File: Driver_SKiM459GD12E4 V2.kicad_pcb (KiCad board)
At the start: 4 copper layers, 169.2 x 116 mm, 339 parts, among them J1 2-338069-0, J13 EL1, J14 GL1, J15 NTC1_A, J16 NTC1_B, J17 GH1, J18 OUT1, J19 CH1, J20 EL2, J21 GL2, J22 NTC2_A, J23 NTC2_B, J24 GH2, J25 OUT2, J26 CH2, J27 EL3, J28 GL3, J29 NTC3_A, J30 NTC3_B, J31 GH3, J32 OUT3, J33 CH3, Q1 MJD44H11T4G, Q10 MJD45H11T4G, Q11 MJD44H11T4G, Q12 MJD45H11T4G, Q2 MJD45H11T4G, Q3 MJD44H11T4G, Q4 MJD45H11T4G, Q5 MJD44H11T4G, Q6 MJD45H11T4G, Q7 MJD44H11T4G, Q8 MJD45H11T4G, Q9 MJD44H11T4G, U1 LM2904, U2 R-785.0-1.0, U3 LM397, U4 HCPL-0611

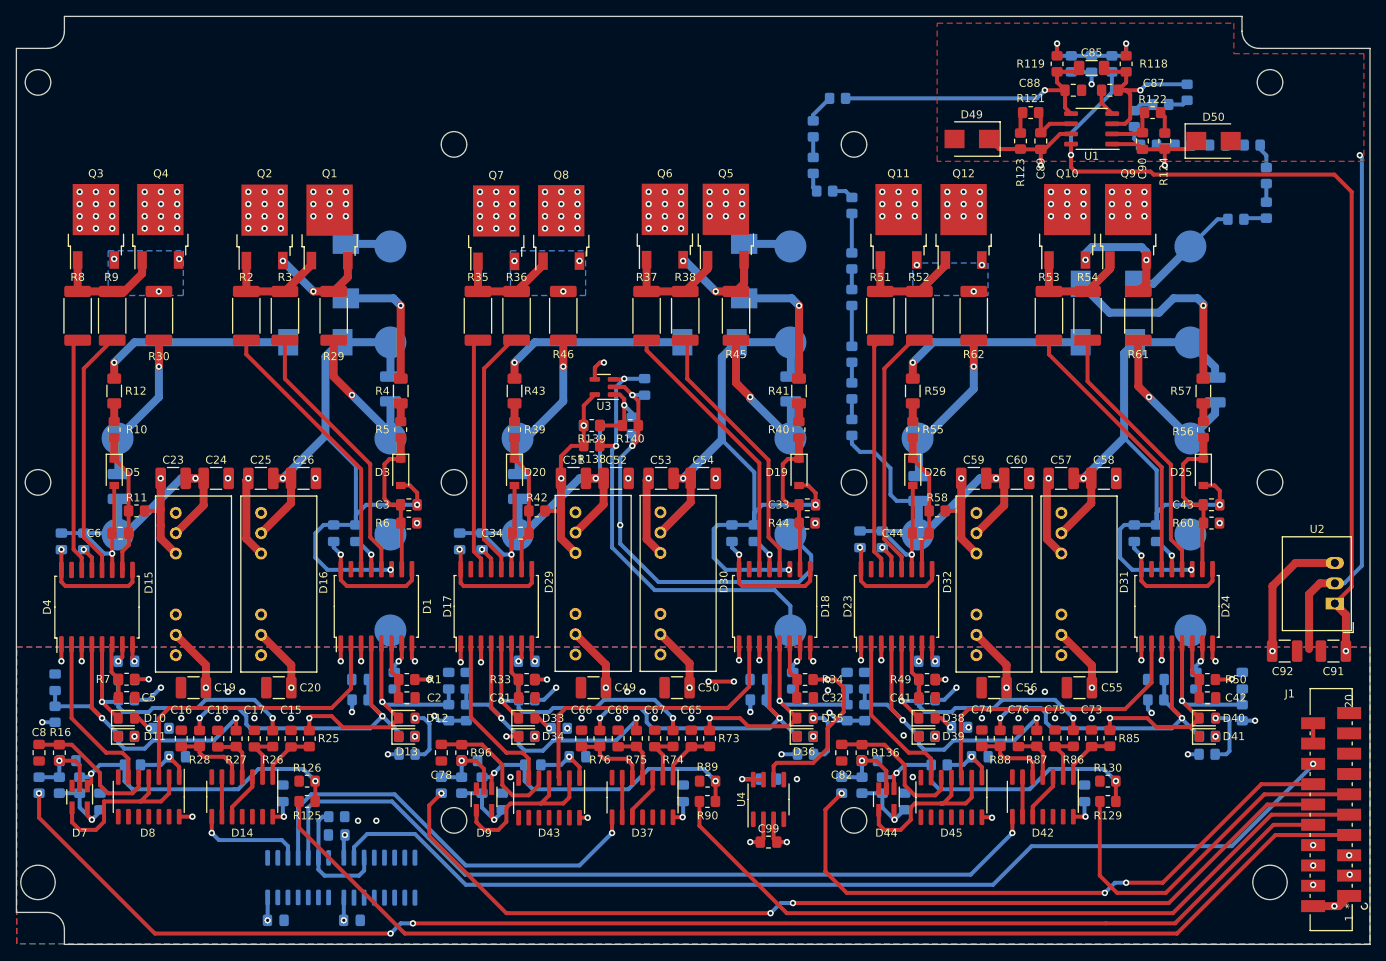
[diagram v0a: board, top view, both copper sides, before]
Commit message: Исправмл логику защиты по температуре
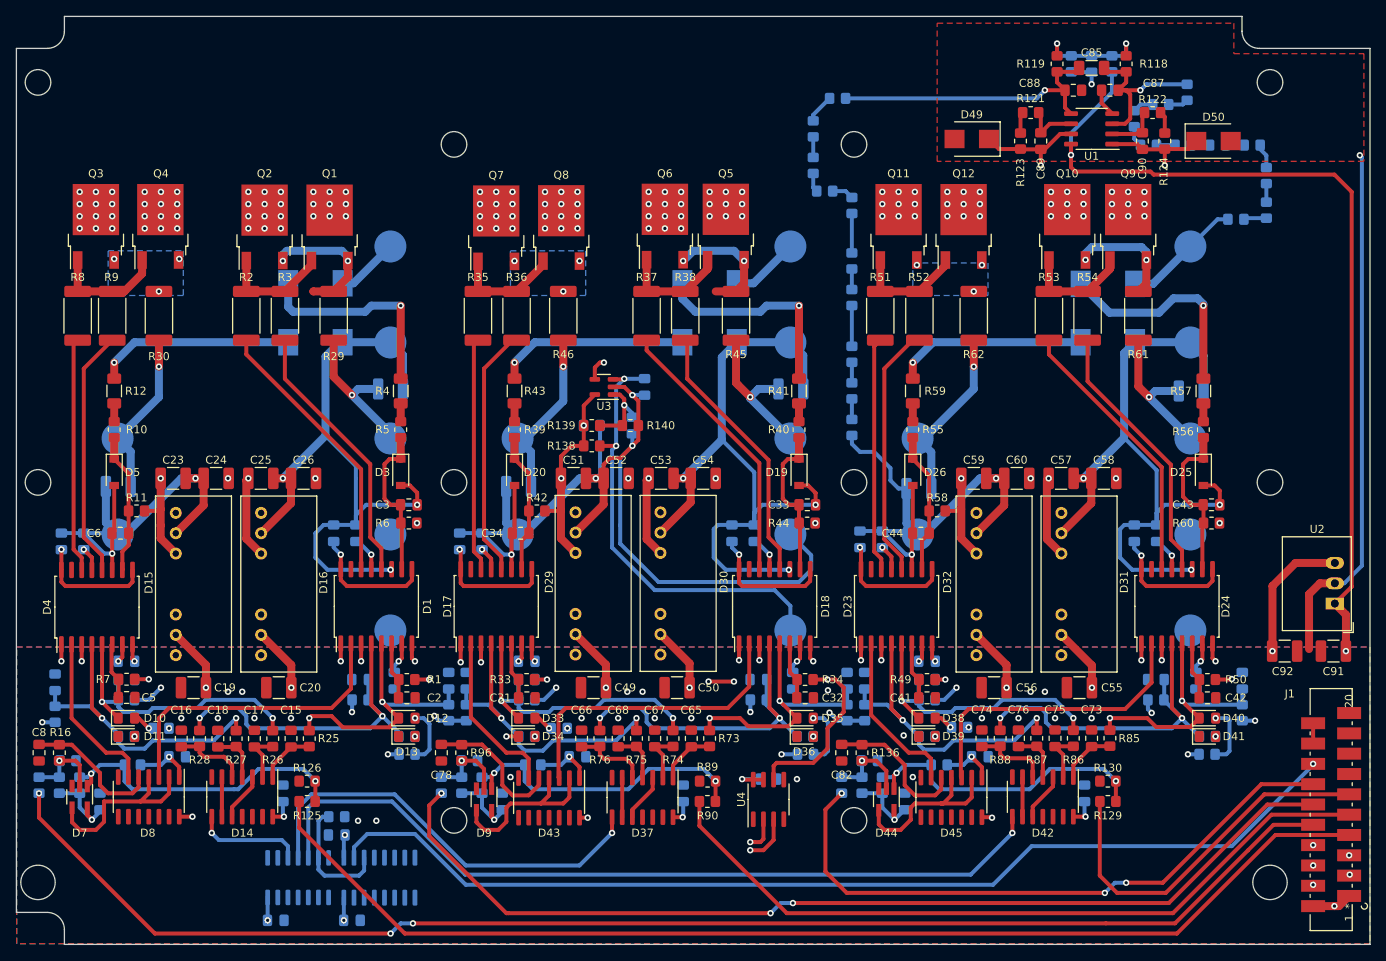
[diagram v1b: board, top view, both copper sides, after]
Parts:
- removed C99: 0.1u, Capacitor_SMD:C_0805_2012Metric_Pad1.18x1.45mm_HandSolder
- moved D21 4.58 mm to (146.8, 68.3), turned to 180 degrees
- moved D2 4.10 mm to (97.5, 68.3), turned to 180 degrees
- moved R63 2.99 mm to (207.0, 81.8), turned to 0 degrees
- turned R31 to 0 degrees
- turned R32 to 180 degrees
- turned R47 to 0 degrees
- turned R48 to 180 degrees
- turned R64 to 180 degrees
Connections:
- U3 pad 4: Net-(C99-Pad1) -> Net-(U4-Pad3)
- U4 pad 2: Net-(C99-Pad1) -> +15V_L2
- U4 pad 3: EL2 -> Net-(U4-Pad3)
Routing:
- net Net-(U4-Pad3): track 0.00 -> 80.1 mm, vias 0 -> 2
- net Net-(C99-Pad1): track 77.2 -> 0.00 mm, vias 2 -> 0
- net +15V_L2: track 28.2 -> 84.3 mm, vias 15 -> 16
- net EL2: track 179.9 -> 124.5 mm, vias 6 -> 4
- net Net-(D2-Pad2): track 16.4 -> 26.7 mm
- net Net-(D21-Pad2): track 16.4 -> 26.6 mm
- net Net-(Q1-Pad3): track 12.5 -> 17.1 mm
- net CH2: track 5.91 -> 9.06 mm
- net Net-(Q5-Pad3): track 12.6 -> 15.6 mm
- net CH1: track 5.70 -> 8.34 mm
- net EL1: track 50.1 -> 52.3 mm
- net OUT1: track 85.8 -> 88.0 mm
- net GL3: track 20.5 -> 22.6 mm
- net GL2: track 19.8 -> 22.0 mm
- net GL1: track 18.9 -> 21.1 mm
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
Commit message: Добавил подтяжку на выход HCPL
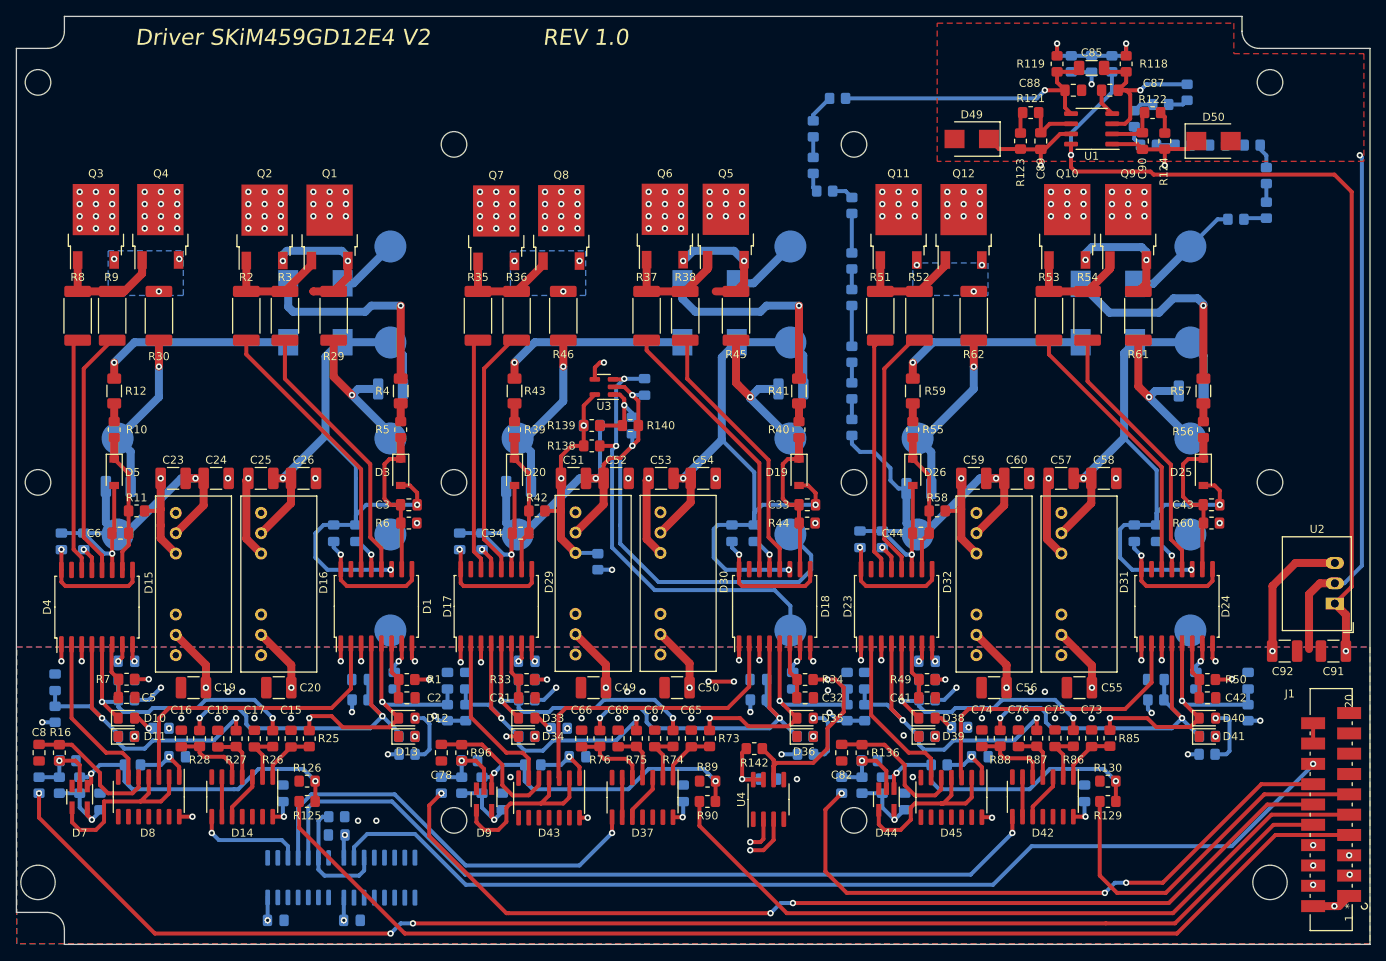
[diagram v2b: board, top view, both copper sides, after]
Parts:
- added R141: 300, Resistor_SMD:R_0805_2012Metric_Pad1.20x1.40mm_HandSolder, B.Cu at (132.8, 103.1)
- added R142: 350, Resistor_SMD:R_0805_2012Metric_Pad1.20x1.40mm_HandSolder, F.Cu at (152.4, 126.5)
- R138, R139: value 120 -> 1k
- moved C71 0.72 mm to (214.1, 118.0)
- moved R81 0.72 mm to (214.1, 122.0)
- moved C13 0.15 mm to (114.0, 118.0)
- moved R21 0.15 mm to (114.0, 122.0)
- moved C62 0.07 mm to (116.3, 118.0)
- moved R68 0.07 mm to (116.3, 122.0)
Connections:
- U4 pad 2: +15V_L2 -> Net-(U4-Pad2)
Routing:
- net +15V_L2: track 84.3 -> 31.1 mm, vias 16 -> 15
- net Net-(U4-Pad2): track 0.00 -> 52.5 mm, vias 0 -> 2
- net RST_H3: track 167.8 -> 172.3 mm
- net +5VD: track 122.3 -> 126.4 mm
- net FLT_H3: track 33.5 -> 34.3 mm
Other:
- board text added: "Driver SKiM459GD12E4 V2"
- board text added: "REV 1.0"

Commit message: Добавил названия элементов в схеме
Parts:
- C85: value C -> 0.1u
- C86, C87, C88, C89, C90: value C_Small -> 1n
- D19, D20, D25, D26, D3, D5: value BZT52C10-7-F -> MMSZ5240B
- D2, D21, D22, D27, D28, D6: value US3M-13 -> MURS360T3G
- D49, D50: value D_Zener_Small -> 1SMB5929BT3G
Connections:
- net RST_H3 renamed RST_H1
